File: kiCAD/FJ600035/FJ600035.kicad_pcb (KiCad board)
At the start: 2 copper layers, 35 x 7.3 mm, 12 parts, among them J1 Conn, J2 Conn, J3 Conn, J4 Conn, J5 Conn, J6 Conn, J7 Conn, J8 Conn, J9 Conn

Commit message: изменено:      kiCAD/FJ600035/FJ600035-cache.lib 	изменено:      kiCAD/FJ600035/FJ600035.kicad_pcb 	изменено:      kiCAD/FJ600035/FJ600035.kicad_pcb-bak 	изменено:      kiCAD/FJ600035/FJ600035.sch 	изменено:      kiCAD/FJ600035/FJ600035.sch-bak
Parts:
- removed D2, D3: FJ60035, My-library:FJ60035
- removed J4, J5, J6, J7, J8, J9: Conn, My-library:SMD-CONN
- added D1: FJ60035, My-library:FJ60035, B.Cu at (39.1, 46.8)
- added J1: Conn, My-library:SMD-CONN, B.Cu at (43.4, 46.9)
- added J2: Conn, My-library:SMD-CONN, B.Cu at (43.4, 44.7)
- added J3: Conn, My-library:SMD-CONN, B.Cu at (43.4, 49.0)
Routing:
- net (no net): track 0.00 -> 30.2 mm
- net Net-(D2-PadA1): track 15.0 -> 0.00 mm
- net Net-(D3-PadA1): track 14.9 -> 0.00 mm
- net Net-(D2-PadC1): track 11.9 -> 0.00 mm
- net Net-(D3-PadC1): track 11.8 -> 0.00 mm
- net Net-(D2-PadC6): track 3.45 -> 0.00 mm
- net Net-(D3-PadC6): track 3.41 -> 0.00 mm
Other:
- board size 35 x 7.3 mm -> 19.8 x 7.3 mm

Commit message: изменено:      kiCAD/FJ600035/FJ600035.kicad_pcb 	новый файл:    kiCAD/FJ600035/FJ600035.kicad_prl 	новый файл:    kiCAD/FJ600035/FJ600035.kicad_pro 	новый файл:    kiCAD/FJ600035/FJ600035.kicad_sch 	изменено:      kiCAD/FJ600035/fp-info-cache 	новый файл:    kiCAD/FJ600035/gerber/FJ600035.zip 	новый файл:    kiCAD/FJ600035/sym-lib-table
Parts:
- removed the D1 at (39.1, 46.8)
- removed the J1 at (43.4, 46.9)
- removed the J2 at (43.4, 44.7)
- removed the J3 at (43.4, 49.0)
- D1: footprint My-library:FJ60035 -> lib:FJ60035
- J1, J2, J3: footprint My-library:SMD-CONN -> lib:conn_mini
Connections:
- net Net-(D1-PadA1) renamed /Catode
- net Net-(D1-PadC1) renamed /Anode
- net Net-(D1-PadC6) renamed /Fast
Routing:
- net (no net): track 30.2 -> 0.00 mm
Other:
- board size 19.8 x 7.3 mm -> 9.4 x 7.3 mm
- net class Default removed

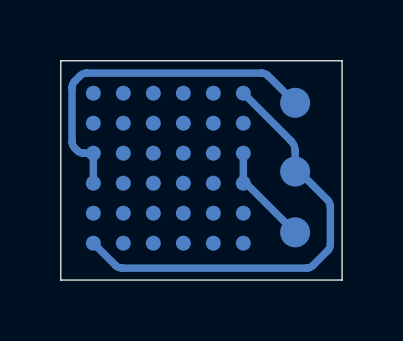
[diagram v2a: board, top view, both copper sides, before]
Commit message: изменено:      Android/AndroidDoZer/app/build/outputs/apk/release/app-release.apk 	удалено:       Android/AndroidDoZer/app/release/app-release.apk 	изменено:      Android/AndroidDoZer/app/src/main/java/ru/starline/dozer/FullscreenActivity.java 	изменено:      Release/all.zip 	изменено:      Release/mk.sh 	изменено:      kiCAD/FJ600035/FJ600035.kicad_pcb 	изменено:      kiCAD/FJ600035/FJ600035.kicad_prl 	изменено:      kiCAD/FJ600035/FJ600035.kicad_pro 	изменено:      stm32Cube/STM32L412K8code/.settings/language.settings.xml
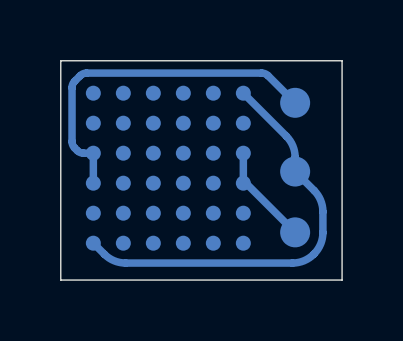
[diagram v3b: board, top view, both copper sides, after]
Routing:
- net /Catode: track 14.9 -> 14.1 mm
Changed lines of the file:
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@@
     (pad_to_mask_clearance 0)
     (pcbplotparams
-      (layerselection 0x0001040_fffffffe)
+      (layerselection 0x0001050_fffffffe)
       (disableapertmacros false)
       (usegerberextensions false)
@@
     (property "Sheetname" "")
     (attr through_hole)
-    (fp_text reference "D1" (at -4.80568 0.9652 180) (layer "B.SilkS")
+    (fp_text reference "D1" (at -4.80568 0.9652 180) (layer "B.SilkS") hide
       (effects (font (size 1 1) (thickness 0.15)) (justify mirror))
     )
-    (fp_text value "FJ60035" (at -0.3 5.25 180) (layer "B.Fab")
+    (fp_text value "FJ60035" (at -0.3 5.25 180) (layer "B.Fab") hide
       (effects (font (size 1 1) (thickness 0.15)) (justify mirror))
     )
@@
     (property "Sheetname" "")
     (attr smd)
-    (fp_text reference "J1" (at 0 0.5 180 unlocked) (layer "B.SilkS")
+    (fp_text reference "J1" (at 0 0.5 180 unlocked) (layer "B.SilkS") hide
       (effects (font (size 1 1) (thickness 0.15)) (justify mirror))
     )
-    (fp_text value "Conn" (at 0 -1 180 unlocked) (layer "B.Fab")
+    (fp_text value "Conn" (at 0 -1 180 unlocked) (layer "B.Fab") hide
       (effects (font (size 1 1) (thickness 0.15)) (justify mirror))
     )
@@
     (property "Sheetname" "")
     (attr smd)
-    (fp_text reference "J2" (at 0 0.5 180 unlocked) (layer "B.SilkS")
+    (fp_text reference "J2" (at 0 0.5 180 unlocked) (layer "B.SilkS") hide
       (effects (font (size 1 1) (thickness 0.15)) (justify mirror))
     )
-    (fp_text value "Conn" (at 0 -1 180 unlocked) (layer "B.Fab")
+    (fp_text value "Conn" (at 0 -1 180 unlocked) (layer "B.Fab") hide
       (effects (font (size 1 1) (thickness 0.15)) (justify mirror))
     )
@@
     (property "Sheetname" "")
     (attr smd)
-    (fp_text reference "J3" (at 0 0.5 180 unlocked) (layer "B.SilkS")
+    (fp_text reference "J3" (at 0 0.5 180 unlocked) (layer "B.SilkS") hide
       (effects (font (size 1 1) (thickness 0.15)) (justify mirror))
     )
-    (fp_text value "Conn" (at 0 -1 180 unlocked) (layer "B.Fab")
+    (fp_text value "Conn" (at 0 -1 180 unlocked) (layer "B.Fab") hide
       (effects (font (size 1 1) (thickness 0.15)) (justify mirror))
     )
@@
   (gr_line (start 25.16124 50.56632) (end 25.16124 43.2562) (layer "Edge.Cuts") (width 0.05))
   (gr_line (start 25.16124 43.2562) (end 34.53892 43.2562) (layer "Edge.Cuts") (width 0.05))
-  (segment (start 31.24772 44.3376) (end 32.827834 45.917714) (width 0.25) (layer "B.Cu") (net 1))
-  (segment (start 32.97428 46.271267) (end 32.97428 46.94936) (width 0.25) (layer "B.Cu") (net 1))
-  (segment (start 34.059892 49.587388) (end 33.565068 50.082212) (width 0.25) (layer "B.Cu") (net 1))
-  (segment (start 32.97428 46.81728) (end 34.059892 47.902892) (width 0.25) (layer "B.Cu") (net 1))
-  (segment (start 26.992332 50.082212) (end 26.24772 49.3376) (width 0.25) (layer "B.Cu") (net 1))
-  (segment (start 33.352936 50.17008) (end 27.204464 50.17008) (width 0.25) (layer "B.Cu") (net 1))
-  (segment (start 34.14776 48.115024) (end 34.14776 49.375256) (width 0.25) (layer "B.Cu") (net 1))
-  (arc (start 33.565068 50.082212) (mid 33.467741 50.147244) (end 33.352936 50.17008) (width 0.25) (layer "B.Cu") (net 1))
-  (arc (start 34.14776 49.375256) (mid 34.124924 49.490061) (end 34.059892 49.587388) (width 0.25) (layer "B.Cu") (net 1))
-  (arc (start 34.059892 47.902892) (mid 34.124924 48.000219) (end 34.14776 48.115024) (width 0.25) (layer "B.Cu") (net 1))
-  (arc (start 32.827834 45.917714) (mid 32.93622 46.079926) (end 32.97428 46.271267) (width 0.25) (layer "B.Cu") (net 1))
-  (arc (start 26.992332 50.082212) (mid 27.089659 50.147244) (end 27.204464 50.17008) (width 0.25) (layer "B.Cu") (net 1))
+  (segment (start 33.9 48.985786) (end 33.9 48.289294) (width 0.25) (layer "B.Cu") (net 1))
+  (segment (start 31.24772 44.3376) (end 32.681387 45.771267) (width 0.25) (layer "B.Cu") (net 1))
+  (segment (start 32.97428 46.478374) (end 32.97428 46.94936) (width 0.25) (layer "B.Cu") (net 1))
+  (segment (start 27.324334 50) (end 32.885786 50) (width 0.25) (layer "B.Cu") (net 1))
+  (segment (start 33.607107 47.582187) (end 32.97428 46.94936) (width 0.25) (layer "B.Cu") (net 1))
+  (segment (start 33.592893 49.707107) (end 33.607107 49.692893) (width 0.25) (layer "B.Cu") (net 1))
+  (segment (start 26.24772 49.3376) (end 26.617227 49.707107) (width 0.25) (layer "B.Cu") (net 1))
+  (arc (start 33.9 48.985786) (mid 33.82388 49.368469) (end 33.607107 49.692893) (width 0.25) (layer "B.Cu") (net 1))
+  (arc (start 33.607107 47.582187) (mid 33.82388 47.90661) (end 33.9 48.289294) (width 0.25) (layer "B.Cu") (net 1))
+  (arc (start 26.617227 49.707107) (mid 26.94165 49.92388) (end 27.324334 50) (width 0.25) (layer "B.Cu") (net 1))
+  (arc (start 33.592893 49.707107) (mid 33.26847 49.92388) (end 32.885786 50) (width 0.25) (layer "B.Cu") (net 1))
+  (arc (start 32.681387 45.771267) (mid 32.89816 46.09569) (end 32.97428 46.478374) (width 0.25) (layer "B.Cu") (net 1))
   (segment (start 31.24772 47.3376) (end 31.3356 47.3376) (width 0.25) (layer "B.Cu") (net 2))
   (segment (start 31.3356 47.3376) (end 32.97428 48.97628) (width 0.25) (layer "B.Cu") (net 2))
